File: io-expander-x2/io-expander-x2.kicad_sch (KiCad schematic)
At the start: 6 parts, among them IC1 MCP23017-E_SO, IC2 MCP23017-E_SO, J1 QWIIC, J2 QWIIC, J3 Screw-8P-5.08-1729186, J4 Screw-8P-5.08-1729186

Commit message: Daughter board is coming along nicely.
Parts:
- added D1: LED, LED_SMD:LED_1206_3216Metric, symbol Device:LED
- added F1: MF-USHT010KX-2, 00_General:FUSC3226X85N, symbol 00_General:MF-USHT010KX-2
- added H1, H2, H3, H4: MountingHole, MountingHole:MountingHole_3.2mm_M3_ISO7380, symbol Mechanical:MountingHole
- added J5, J6: Screw-8P-5.08-1729186, 00_Connectors:Screw-8P-5.08-1729186, symbol 00_Connectors:Screw-8P-5.08-1729186
- added R1: R, Resistor_SMD:R_0805_2012Metric, symbol Device:R
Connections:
- new net: D1.2 (A), R1.2
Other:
- moved on the sheet: J4

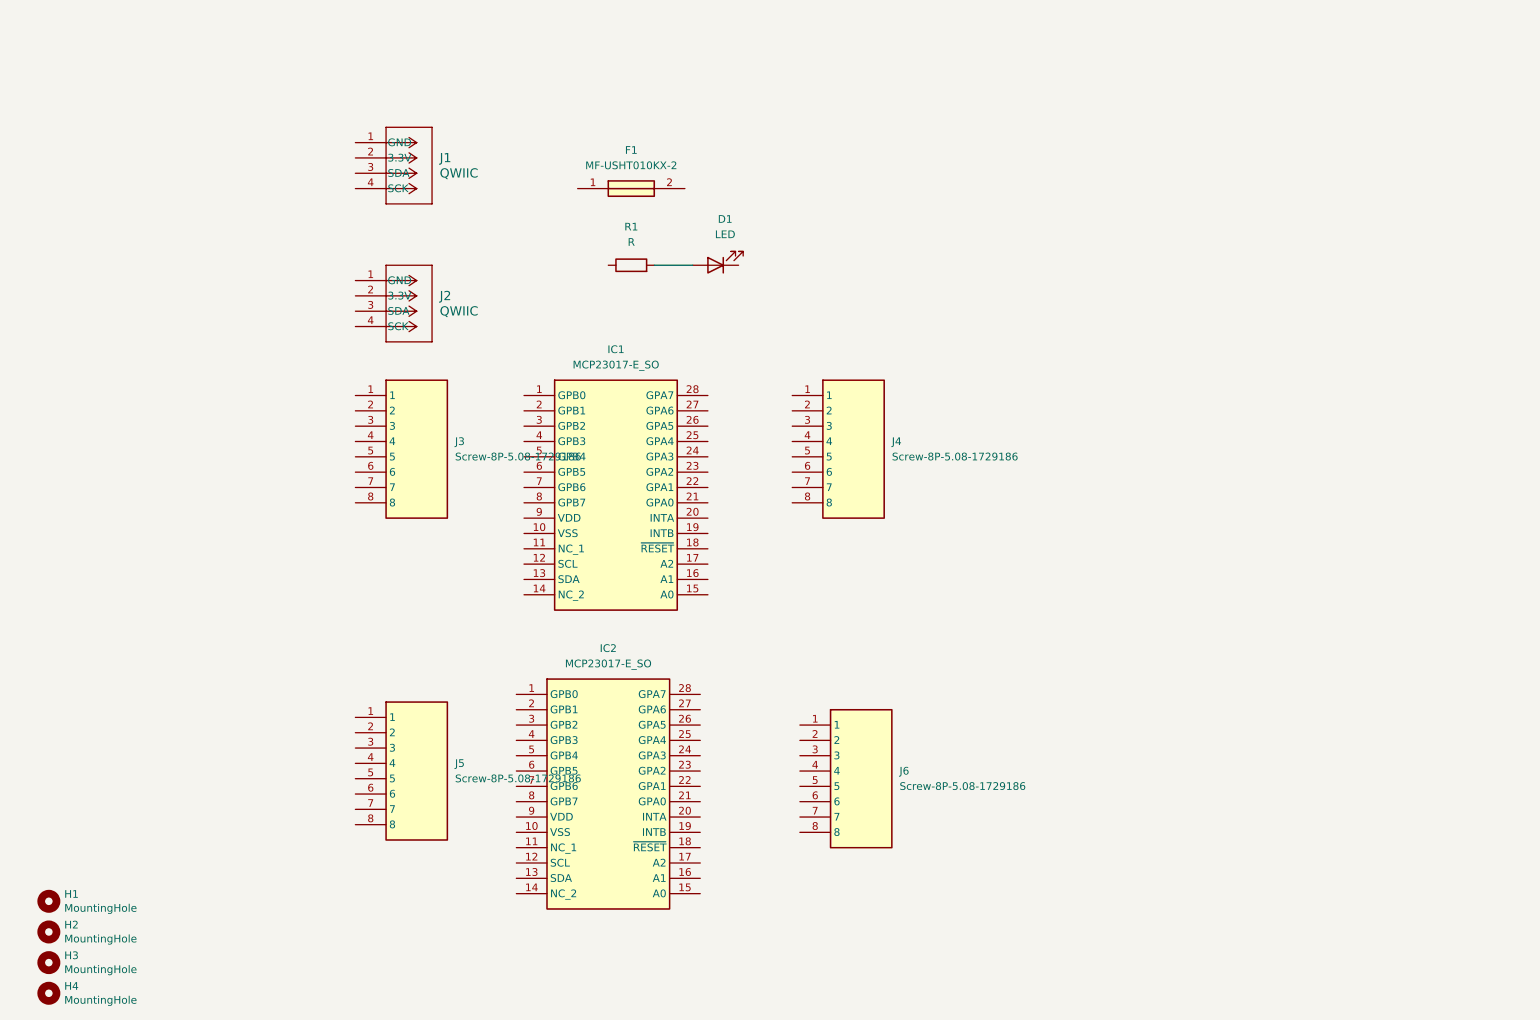
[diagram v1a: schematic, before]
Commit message: Most components are now placed. The schematic has a lot of the wiring done. Need to transfer it onto the PCB once I figure out how I will wire up the address lines.
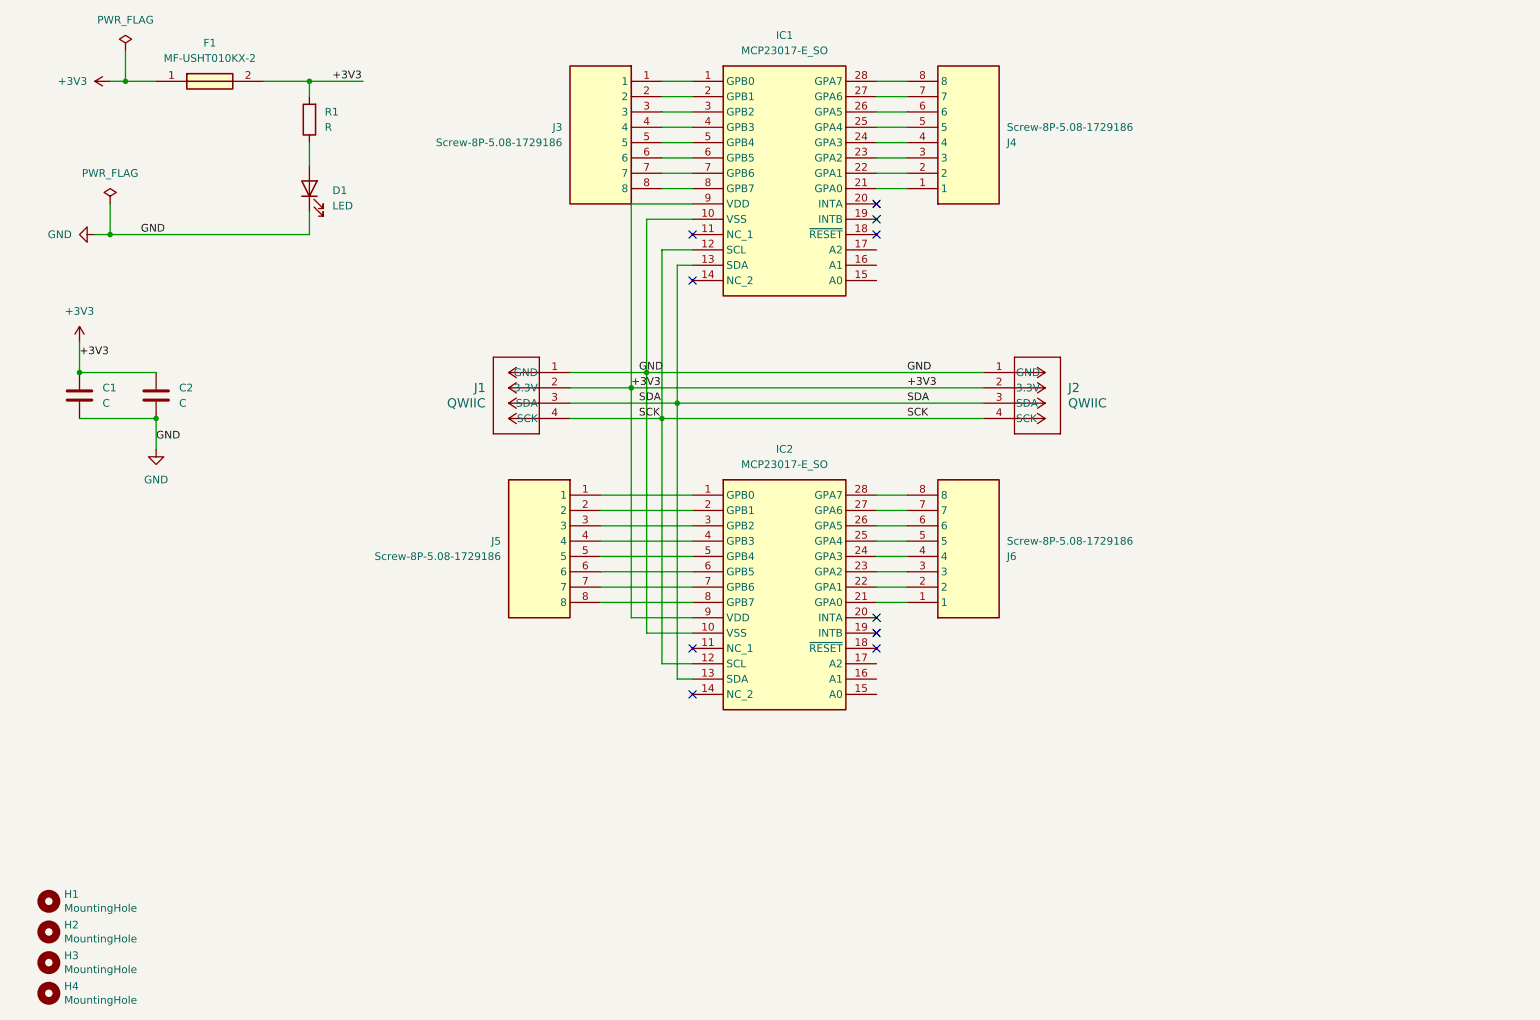
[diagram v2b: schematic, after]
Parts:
- added C1, C2: C, Capacitor_SMD:C_0805_2012Metric_Pad1.18x1.45mm_HandSolder, symbol Device:C
- IC1, IC2: footprint SOIC127P1030X265-28N -> 00_General:MCP23017-E-SO
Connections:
- net at IC1.1 (GPB0): now also J3.1
- net GND: now reaches IC1.10 (VSS)
- net GND: now also D1.1 (K), IC2.10 (VSS), J1.1 (GND), J2.1 (GND), C1.2, C2.2
- net SCK: now reaches IC1.12 (SCL)
- net SCK: now also IC2.12 (SCL), J1.4 (SCK), J2.4 (SCK)
- net SDA: now reaches IC1.13 (SDA)
- net SDA: now also IC2.13 (SDA), J1.3 (SDA), J2.3 (SDA)
- net at IC1.2 (GPB1): now also J3.2
- net at IC1.21 (GPA0): now also J4.1
- net at IC1.22 (GPA1): now also J4.2
- net at IC1.23 (GPA2): now also J4.3
- net at IC1.24 (GPA3): now also J4.4
- net at IC1.25 (GPA4): now also J4.5
- net at IC1.26 (GPA5): now also J4.6
- net at IC1.27 (GPA6): now also J4.7
- net at IC1.28 (GPA7): now also J4.8
- net at IC1.3 (GPB2): now also J3.3
- net at IC1.4 (GPB3): now also J3.4
- net at IC1.5 (GPB4): now also J3.5
- net at IC1.6 (GPB5): now also J3.6
- net at IC1.7 (GPB6): now also J3.7
- net at IC1.8 (GPB7): now also J3.8
- net +3V3: now reaches IC1.9 (VDD)
- net +3V3: now also F1.1, F1.2, IC2.9 (VDD), J1.2 (3.3V), J2.2 (3.3V), R1.2, C1.1, C2.1
- net at IC2.1 (GPB0): now also J5.1
- net at IC2.2 (GPB1): now also J5.2
- net at IC2.21 (GPA0): now also J6.1
- net at IC2.22 (GPA1): now also J6.2
- net at IC2.23 (GPA2): now also J6.3
- net at IC2.24 (GPA3): now also J6.4
- net at IC2.25 (GPA4): now also J6.5
- net at IC2.26 (GPA5): now also J6.6
- net at IC2.27 (GPA6): now also J6.7
- net at IC2.28 (GPA7): now also J6.8
- net at IC2.3 (GPB2): now also J5.3
- net at IC2.4 (GPB3): now also J5.4
- net at IC2.5 (GPB4): now also J5.5
- net at IC2.6 (GPB5): now also J5.6
- net at IC2.7 (GPB6): now also J5.7
- net at IC2.8 (GPB7): now also J5.8
- net at R1.1: now also D1.2 (A)
- no-connect marks 0 -> 10
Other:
- moved on the sheet: D1, F1, IC1, IC2, J1, J2, J3, J4, J5, J6, R1

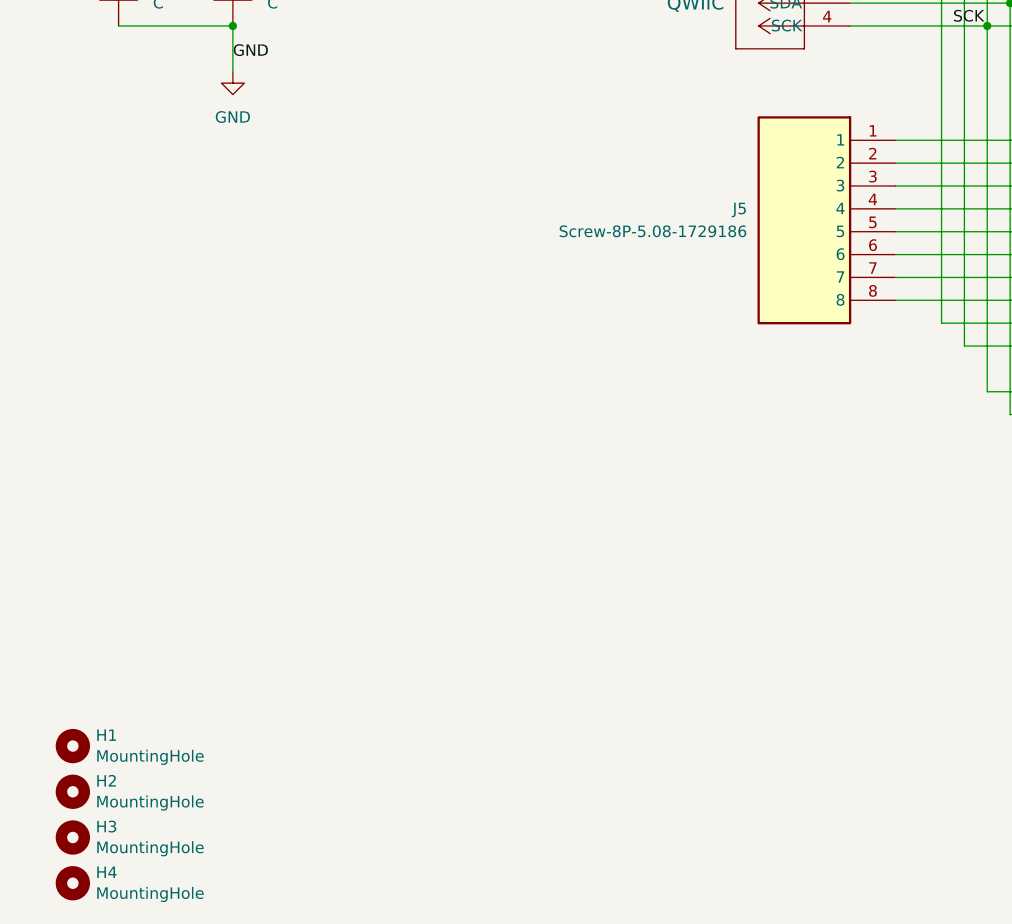
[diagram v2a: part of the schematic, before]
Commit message: Added ground connectors. Board is overly tight now.
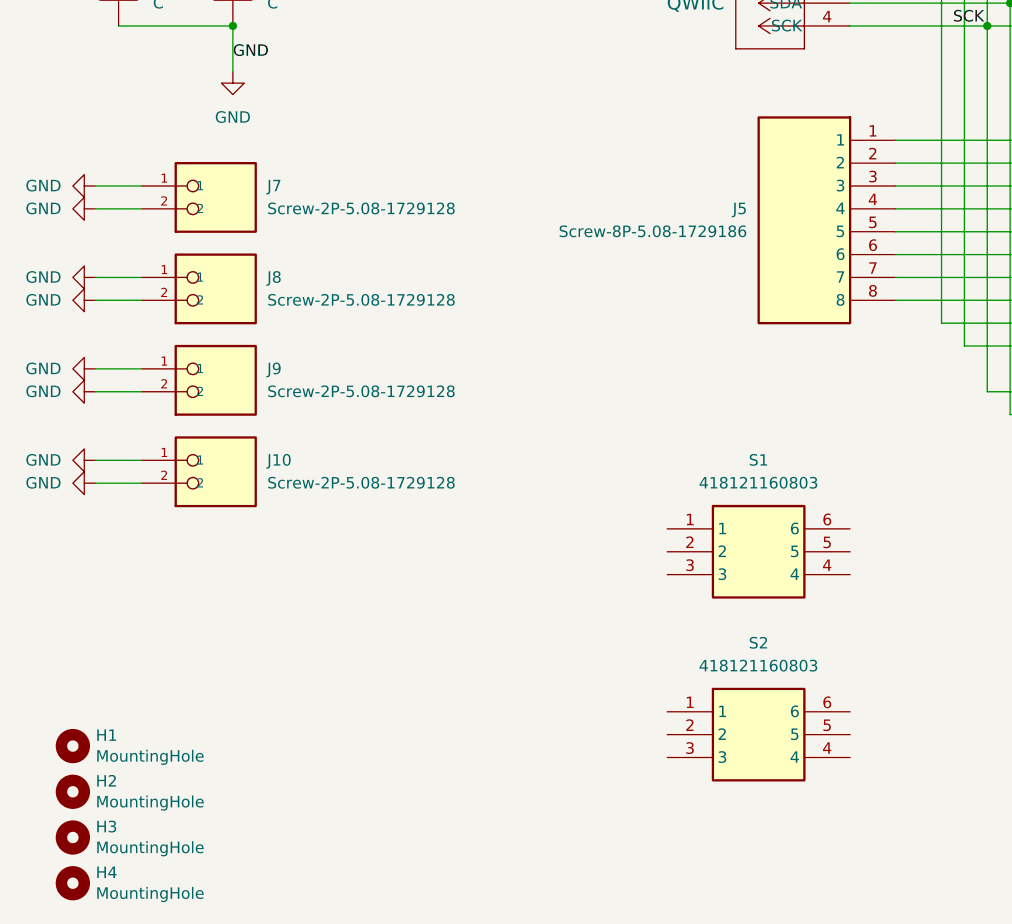
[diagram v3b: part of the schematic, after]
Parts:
- added J10, J7, J8, J9: Screw-2P-5.08-1729128, 00_Connectors:Screw-2P-5.08-1729128, symbol 00_Connectors:Screw-2P-5.08-1729128
- added S1, S2: 418121160803, 00_General:SOP254P980X300-6N, symbol 00_General:418121160803
- H1, H2, H3, H4: footprint MountingHole:MountingHole_3.2mm_M3_ISO7380 -> MountingHole:MountingHole_2.2mm_M2
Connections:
- net GND: now also J10.1, J10.2, J7.1, J7.2, J8.1, J8.2, J9.1, J9.2

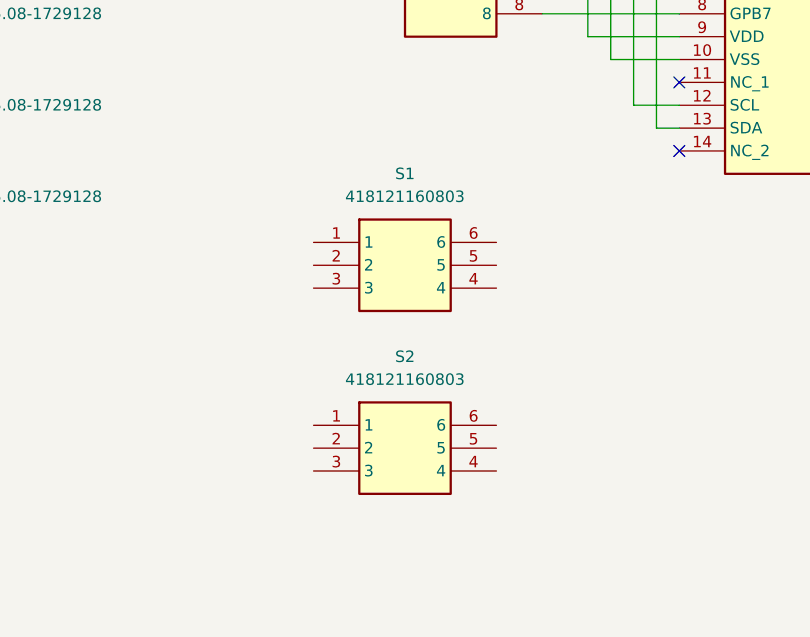
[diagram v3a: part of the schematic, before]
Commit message: Going to use 3x3 header block instead.
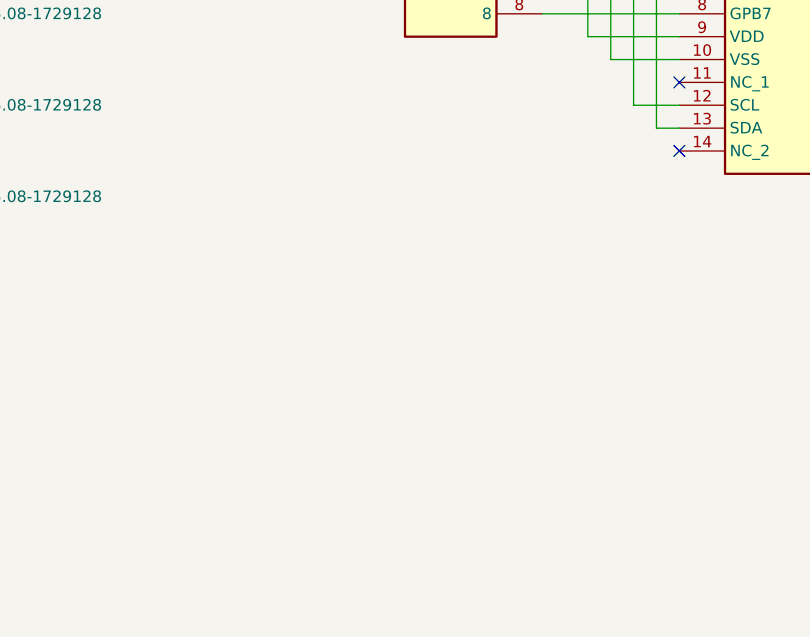
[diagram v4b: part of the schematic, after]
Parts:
- removed S1, S2: 418121160803, 00_General:SOP254P980X300-6N, symbol 00_General:418121160803

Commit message: Minor changes.
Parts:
- removed J10, J7, J8, J9: Screw-2P-5.08-1729128, 00_Connectors:Screw-2P-5.08-1729128, symbol 00_Connectors:Screw-2P-5.08-1729128
- F1: footprint 00_General:FUSC3226X85N -> 00_general:FUSC3226X85N
- IC1, IC2: footprint 00_General:MCP23017-E-SO -> 00_general:MCP23017-E-SO
- J1, J2: footprint 00_Connectors:QWIIC -> 00_connectors:QWIIC
- J3, J4, J5, J6: value Screw-8P-5.08-1729186 -> 8 Position Screw Terminal; footprint 00_Connectors:Screw-8P-5.08-1729186 -> 00_connectors:PHOENIX_1869279

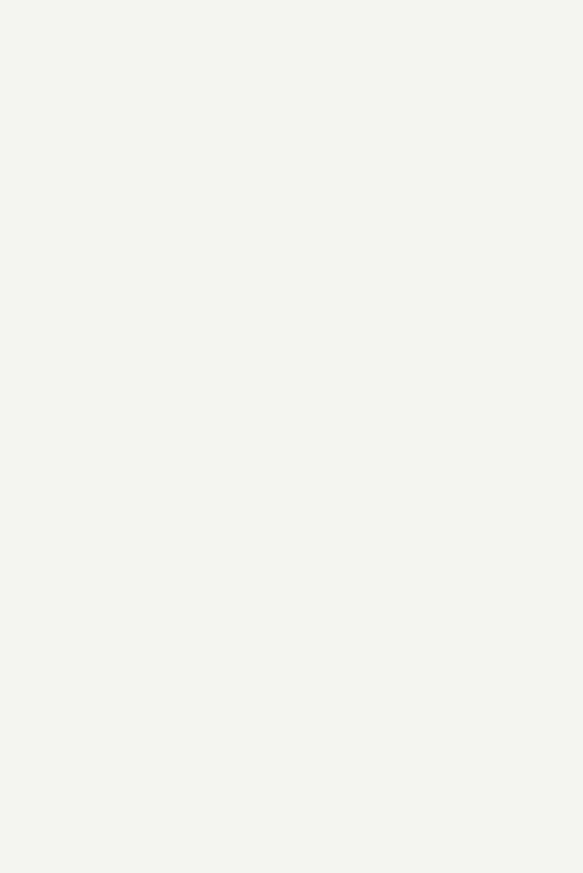
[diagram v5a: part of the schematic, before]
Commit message: Board is larger. Rotated 90 degrees. New connector types selected.
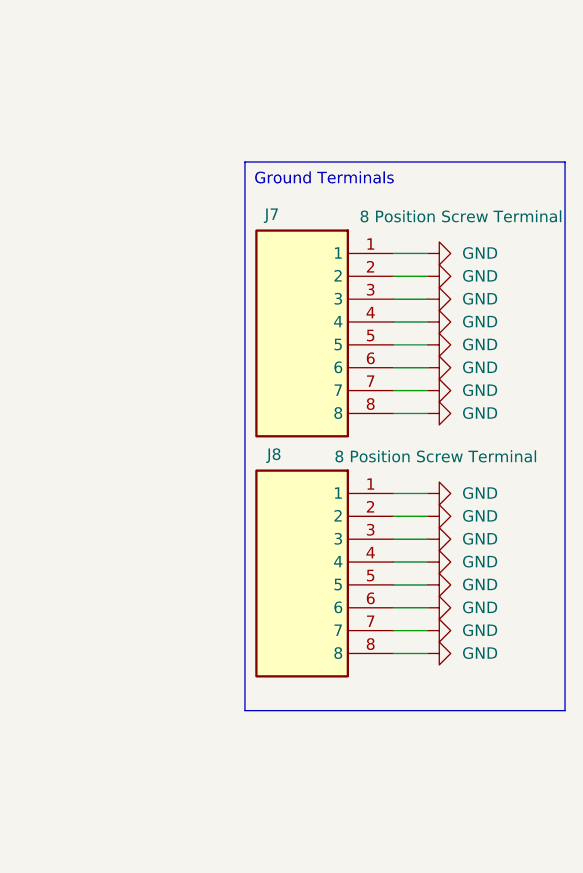
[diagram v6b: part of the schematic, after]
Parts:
- added J7, J8: 8 Position Screw Terminal, 00_connectors:PHOENIX_1869279, symbol 00_Connectors:Screw-8P-5.08-1729186
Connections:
- net GND: now also J7.1, J7.2, J7.3, J7.4, J7.5, J7.6, J7.7, J7.8, J8.1, J8.2, J8.3, J8.4, J8.5, J8.6, J8.7, J8.8
